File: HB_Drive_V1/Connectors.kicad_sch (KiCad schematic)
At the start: 47 parts, among them J501 54-00164, J502 5227699-1, J503 USB-B-S-X-X-VT, J504 Conn_01x06, U501 REF102CU, U502 R-78E5.0-0.5, U503 TL082, U504 TL082, U505 TMH 0515D, U506 AMS1117-3.3

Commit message: commits latest kiCAD project for BOM generation
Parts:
- J502: footprint 5227699-1:TE_5227699-1 -> 5227699:TE_5227699-1
- R501: value 470Ω -> 500Ω
- R503: value 10Ω -> 100Ω
- R505: value 470Ω -> 330Ω
- R507, R508: value 470Ω -> 1KΩ
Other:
- moved on the sheet: D502
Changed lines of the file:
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@@
 	(wire
 		(pts
-			(xy 127 171.45) (xy 127 175.26)
+			(xy 127 172.72) (xy 127 176.53)
 		)
 		(stroke
@@
 	(symbol
 		(lib_id "Device:R_Small_US")
-		(at 127 177.8 180)
+		(at 127 179.07 180)
 		(unit 1)
 		(body_style 1)
@@
 		(dnp no)
 		(property "Reference" "R503"
-			(at 125.73 173.99 90)
+			(at 125.73 175.26 90)
 			(hide yes)
 			(show_name no)
@@
 			)
 		)
-		(property "Value" "10Ω"
-			(at 122.682 177.8 0)
+		(property "Value" "100Ω"
+			(at 122.682 179.07 0)
 			(show_name no)
 			(do_not_autoplace no)
@@
 		)
 		(property "Footprint" "Resistor_SMD:R_0603_1608Metric_Pad0.98x0.95mm_HandSolder"
-			(at 127 177.8 0)
+			(at 127 179.07 0)
 			(hide yes)
 			(show_name no)
@@
 		)
 		(property "Datasheet" ""
-			(at 127 177.8 0)
+			(at 127 179.07 0)
 			(hide yes)
 			(show_name no)
@@
 		)
 		(property "Description" "Resistor, small US symbol"
-			(at 127 177.8 0)
+			(at 127 179.07 0)
 			(hide yes)
 			(show_name no)
@@
 	(symbol
 		(lib_id "Device:LED")
-		(at 127 184.15 270)
+		(at 127 185.42 270)
 		(mirror x)
 		(unit 1)
@@
 		(dnp no)
 		(property "Reference" "D502"
-			(at 131.572 184.912 90)
+			(at 131.572 186.182 90)
 			(show_name no)
 			(do_not_autoplace no)
@@
 		)
 		(property "Value" "GREEN [XL-2012UGC]"
-			(at 138.684 187.452 90)
+			(at 138.684 188.722 90)
 			(show_name no)
 			(do_not_autoplace no)
@@
 		)
 		(property "Footprint" "LED_SMD:LED_0805_2012Metric_Pad1.15x1.40mm_HandSolder"
-			(at 127 184.15 0)
+			(at 127 185.42 0)
 			(hide yes)
 			(show_name no)
@@
 		)
 		(property "Datasheet" ""
-			(at 127 184.15 0)
+			(at 127 185.42 0)
 			(hide yes)
 			(show_name no)
@@
 		)
 		(property "Description" "Light emitting diode"
-			(at 127 184.15 0)
+			(at 127 185.42 0)
 			(hide yes)
 			(show_name no)
@@
 		)
 		(property "Sim.Pins" "1=K 2=A"
-			(at 127 184.15 0)
+			(at 127 185.42 0)
 			(hide yes)
 			(show_name no)
@@
 			)
 		)
-		(property "Value" "470Ω"
+		(property "Value" "1KΩ"
 			(at 205.232 177.8 0)
 			(show_name no)
@@
 			)
 		)
-		(property "Value" "470Ω"
+		(property "Value" "500Ω"
 			(at 96.012 179.07 0)
 			(show_name no)
@@
 			)
 		)
-		(property "Value" "470Ω"
+		(property "Value" "330Ω"
 			(at 150.622 177.8 0)
 			(show_name no)
@@
 	(symbol
 		(lib_id "power:GND")
-		(at 127 187.96 0)
+		(at 127 189.23 0)
 		(unit 1)
 		(body_style 1)
@@
 		(dnp no)
 		(property "Reference" "#PWR0513"
-			(at 127 194.31 0)
+			(at 127 195.58 0)
 			(hide yes)
 			(show_name no)
@@
 		)
 		(property "Value" "GND"
-			(at 123.952 191.516 0)
+			(at 123.952 192.786 0)
 			(show_name no)
 			(do_not_autoplace no)
@@
 		)
 		(property "Footprint" ""
-			(at 127 187.96 0)
+			(at 127 189.23 0)
 			(hide yes)
 			(show_name no)
@@
 		)
 		(property "Datasheet" ""
-			(at 127 187.96 0)
+			(at 127 189.23 0)
 			(hide yes)
 			(show_name no)
@@
 		)
 		(property "Description" "Power symbol creates a global label with name \"GND\" , ground"
-			(at 127 187.96 0)
+			(at 127 189.23 0)
 			(hide yes)
 			(show_name no)
@@
 	(symbol
 		(lib_id "power:+3.3V")
-		(at 127 171.45 0)
+		(at 127 172.72 0)
 		(unit 1)
 		(body_style 1)
@@
 		(dnp no)
 		(property "Reference" "#PWR0512"
-			(at 127 175.26 0)
+			(at 127 176.53 0)
 			(hide yes)
 			(show_name no)
@@
 		)
 		(property "Value" "+3.3V"
-			(at 129.286 167.64 0)
+			(at 129.286 168.91 0)
 			(show_name no)
 			(do_not_autoplace no)
@@
 		)
 		(property "Footprint" ""
-			(at 127 171.45 0)
+			(at 127 172.72 0)
 			(hide yes)
 			(show_name no)
@@
 		)
 		(property "Datasheet" ""
-			(at 127 171.45 0)
+			(at 127 172.72 0)
 			(hide yes)
 			(show_name no)
@@
 		)
 		(property "Description" "Power symbol creates a global label with name \"+3.3V\""
-			(at 127 171.45 0)
+			(at 127 172.72 0)
 			(hide yes)
 			(show_name no)
@@
 			)
 		)
-		(property "Value" "470Ω"
+		(property "Value" "1KΩ"
 			(at 178.562 177.8 0)
 			(show_name no)
@@
 			)
 		)
-		(property "Footprint" "5227699-1:TE_5227699-1"
+		(property "Footprint" "5227699:TE_5227699-1"
 			(at 285.75 138.43 0)
 			(hide yes)

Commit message: updates board to REV 1 Ordered version
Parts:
- removed D506: 1N5819WS, Diode_SMD:D_SOD-323, symbol Diode:1N5819WS
- added unit 1 of U504
- C501, C505, C508, C509, C510: value 10uF -> 10uF 10%
- C511: value 22uF -> 10uF 10%
- D501, D502: value GREEN [XL-2012UGC] -> LTST-C170KGKT [GREEN]
- D503, D504, D505: value RED [XL-2012SURC] -> LTST-C170KRKT [RED]
- R502, R504: value 10KΩ -> 10kΩ 1%
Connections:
- net +5V: now also J503.01 (VCC); no longer C510.1, U506.3 (VI)
- net +9V: now also C510.1, U506.3 (VI)
- net GND: now also U504.3 (+)
- new net: U504.1, U504.2 (-)
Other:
- note added: "unused OpAmp 504A on TL082 Dual Package"
- moved on the sheet: TP509, TP510

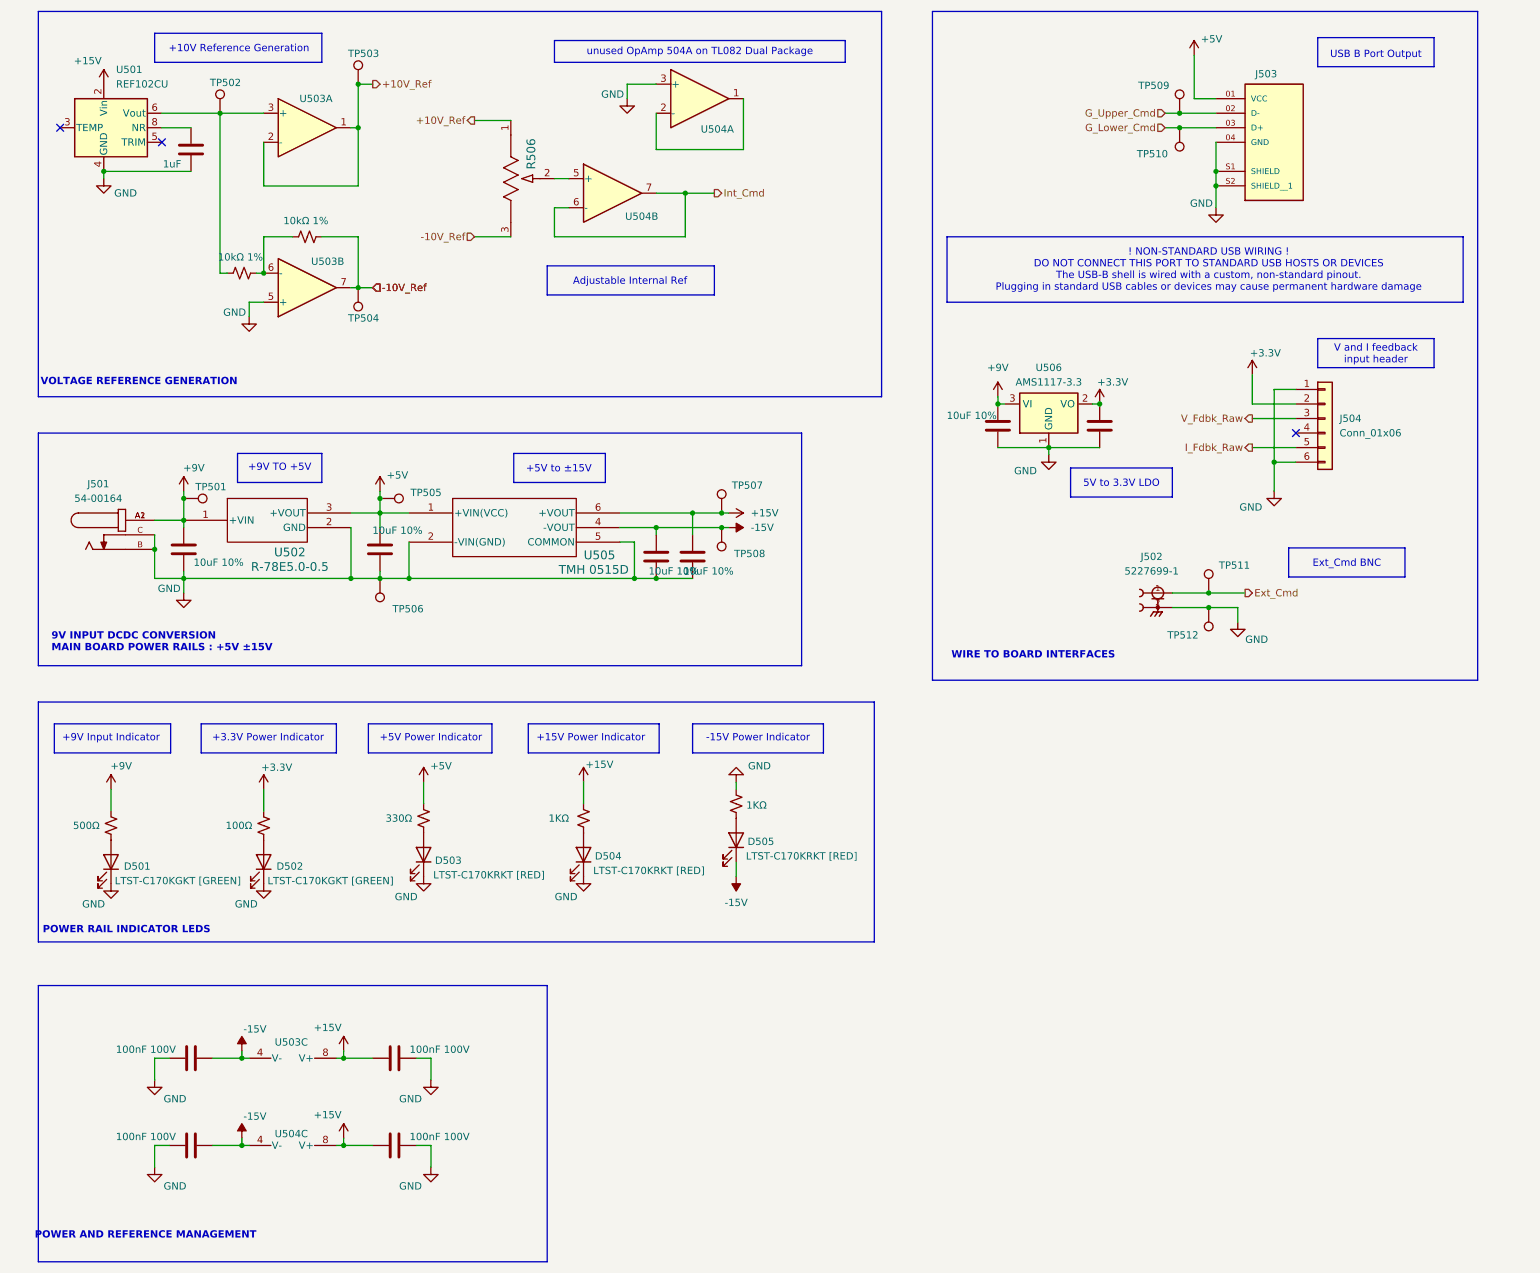
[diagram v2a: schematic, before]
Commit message: Annotates Schematic! Fixes REV1 wiring swaps and replaces buffer
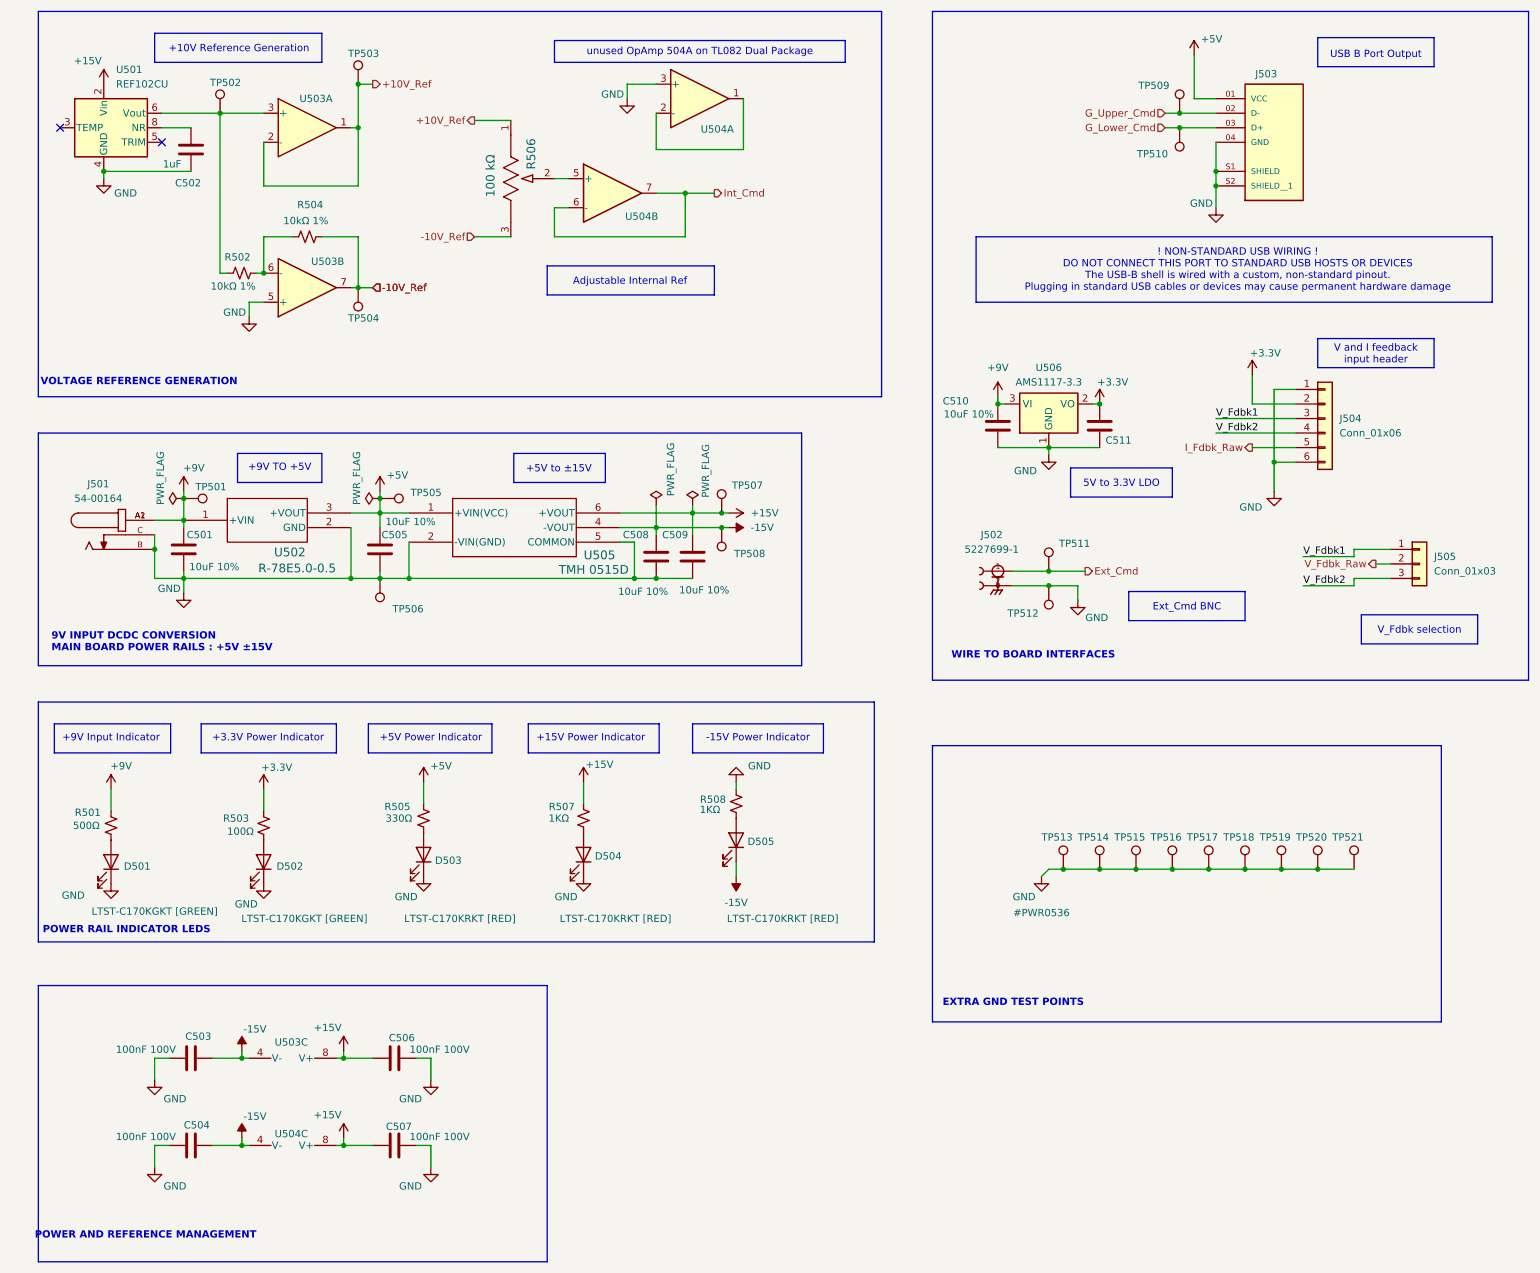
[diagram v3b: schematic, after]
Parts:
- added J505: Conn_01x03, symbol Connector_Generic:Conn_01x03
- added TP513, TP514, TP515, TP516, TP517, TP518, TP519, TP520, TP521: TestPoint, TestPoint:TestPoint_Loop_D2.60mm_Drill1.6mm_Beaded, symbol Connector:TestPoint
- R506: value PV36W104C01B00 -> 100 kΩ
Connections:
- net GND: now also TP513.1, TP514.1, TP515.1, TP516.1, TP517.1, TP518.1, TP519.1, TP520.1, TP521.1
- net V_Fdbk_Raw: now also J505.2 (Pin_2); no longer J504.3 (Pin_3)
- net V_Fdbk2: now reaches J504.4 (Pin_4)
- net V_Fdbk2: now also J505.3 (Pin_3)
- new net V_Fdbk1: J504.3 (Pin_3), J505.1 (Pin_1)
- no-connect marks 3 -> 2
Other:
- note added: "EXTRA GND TEST POINTS"
- note added: "V_Fdbk selection"
- moved on the sheet: J502, TP511, TP512

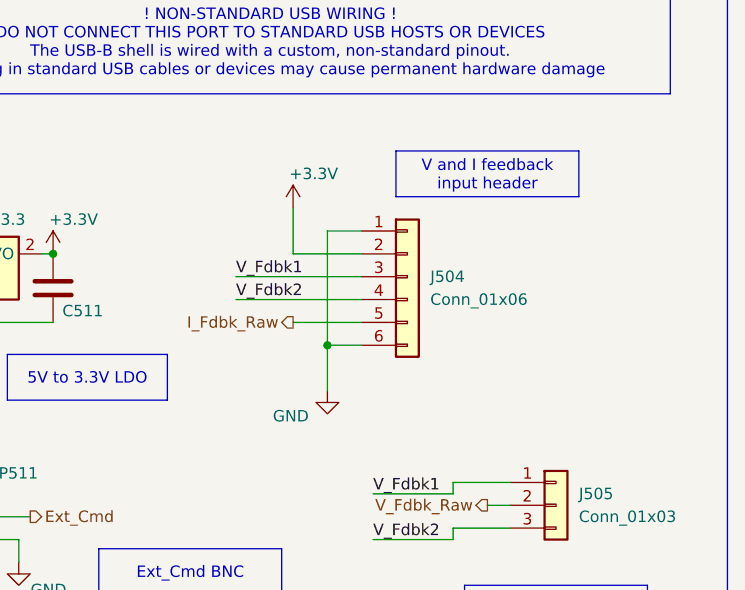
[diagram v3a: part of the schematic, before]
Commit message: annotates PCB! wiring is still broken here
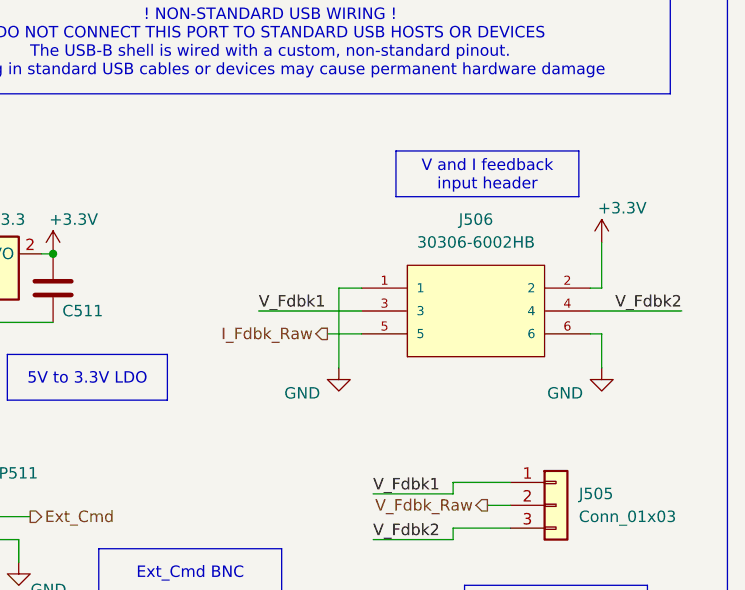
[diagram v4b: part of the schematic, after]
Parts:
- removed J504: Conn_01x06, Connector_PinHeader_2.54mm:PinHeader_1x06_P2.54mm_Vertical, symbol Connector_Generic:Conn_01x06
- added J506: 30306-6002HB, 30306_6002:30306-6002HB, symbol 30306-6002HB:30306-6002HB
- J505: footprint (none) -> Connector_PinHeader_2.54mm:PinHeader_1x03_P2.54mm_Vertical
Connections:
- net +3.3V: now also J506.2
- net GND: now also J506.1, J506.6
- net I_Fdbk_Raw: now also J506.5
- net V_Fdbk1: now also J506.3
- net V_Fdbk2: now also J506.4
